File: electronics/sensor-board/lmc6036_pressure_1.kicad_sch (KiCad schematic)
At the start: 13 parts

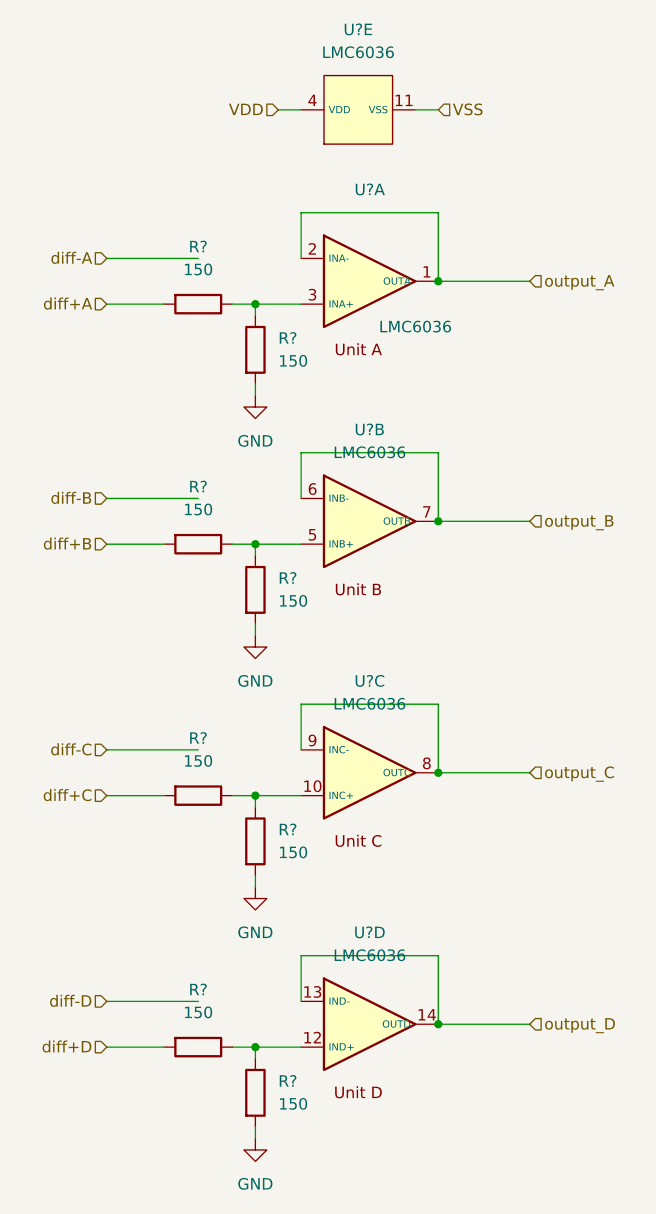
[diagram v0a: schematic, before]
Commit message: work on sensor-board
added MCP960 footprint
finished MCP960 array schematic
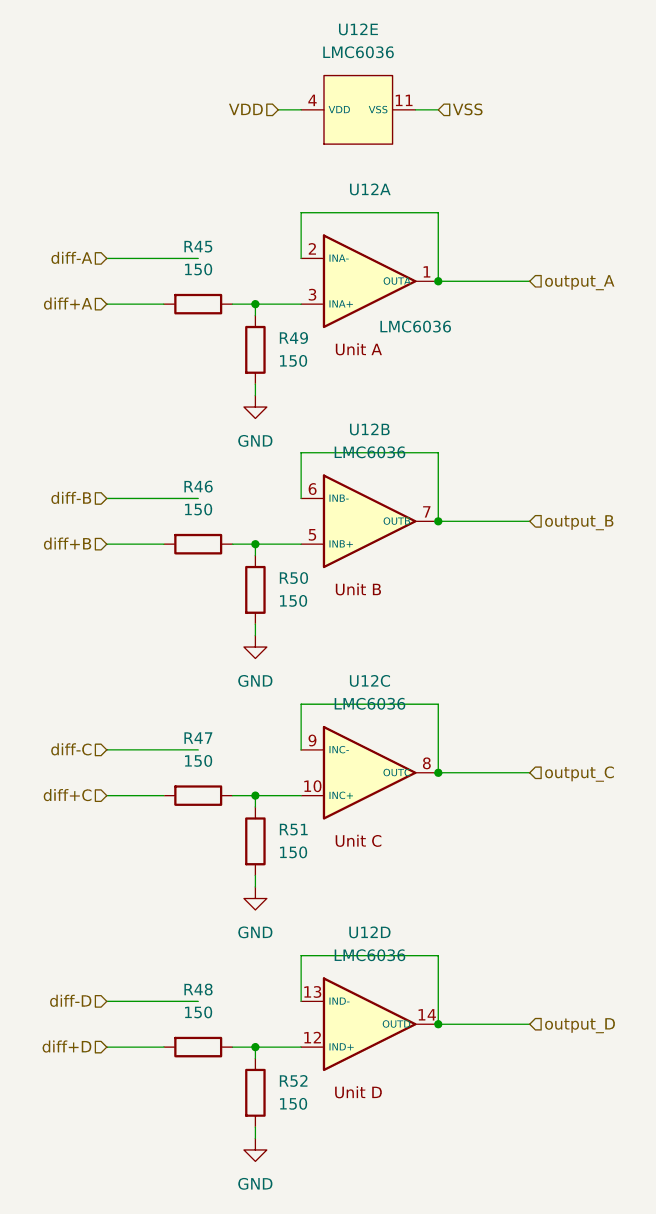
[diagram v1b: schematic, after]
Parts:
- R45, R46, R47, R48, R49, R50, R51, R52: renamed from R?; footprint (none) -> Resistor_SMD:R_0603_1608Metric
- gave numbers to parts that had none: 1
